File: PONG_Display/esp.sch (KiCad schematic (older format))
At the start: 13 parts, among them J8 ESP_Conn, J9 ESP_Prog_Conn, SW2 SW_Push, SW3 SW_Push_SPDT, SW4 SW_Push_SPDT

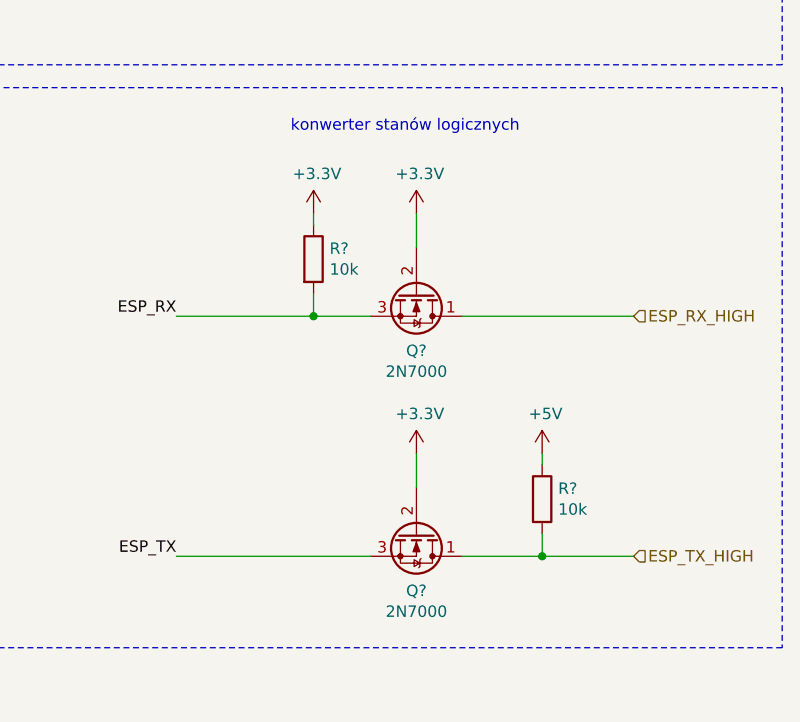
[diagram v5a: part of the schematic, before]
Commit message: dodalem rezystory i wywalilem ze zlacza zasilanie tasmy
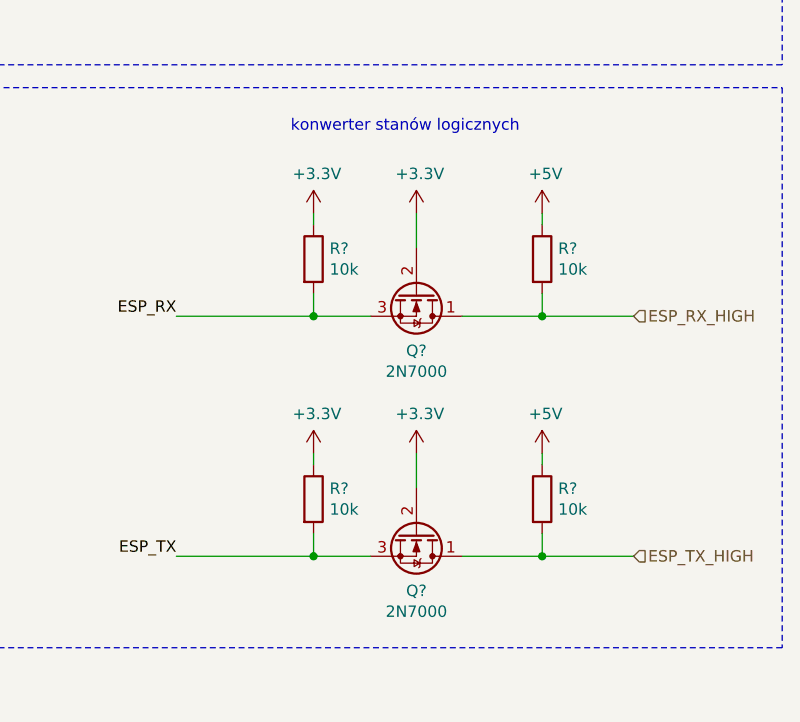
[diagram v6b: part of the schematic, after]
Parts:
- added R? (x2): 10k, Resistor_SMD:R_1206_3216Metric_Pad1.42x1.75mm_HandSolder, symbol Device:R
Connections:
- net +3V3: now also R?.1
- net +5V: now also R?.1
- net ESP_RX_HIGH: now also R?.2
- net ESP_TX: now also R?.2
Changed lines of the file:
@@
 Text Label 4350 3150 2    50   ~ 0
 ESP_RX
+$Comp
+L power:+3.3V #PWR?
+U 1 1 5E9DD25C
+P 4700 5250
+F 0 "#PWR?" H 4700 5100 50  0001 C CNN
+F 1 "+3.3V" H 4715 5423 50  0000 C CNN
+F 2 "" H 4700 5250 50  0001 C CNN
+F 3 "" H 4700 5250 50  0001 C CNN
+	1    4700 5250
+	1    0    0    -1
+$EndComp
+Wire Wire Line
+	4550 5250 4700 5250
+Wire Wire Line
+	4700 5250 4800 5250
+Connection ~ 4700 5250
 Text HLabel 10050 5050 2    50   Input ~ 0
 ESP_RX_HIGH
@@
 Text Label 8050 6100 2    50   ~ 0
 ESP_TX
+$Comp
+L power:+3.3V #PWR?
+U 1 1 5E9E0D36
+P 9100 4600
+F 0 "#PWR?" H 9100 4450 50  0001 C CNN
+F 1 "+3.3V" H 9115 4773 50  0000 C CNN
+F 2 "" H 9100 4600 50  0001 C CNN
+F 3 "" H 9100 4600 50  0001 C CNN
+	1    9100 4600
+	1    0    0    -1
+$EndComp
+$Comp
+L power:+3.3V #PWR?
+U 1 1 5E9E0F18
+P 9100 5650
+F 0 "#PWR?" H 9100 5500 50  0001 C CNN
+F 1 "+3.3V" H 9115 5823 50  0000 C CNN
+F 2 "" H 9100 5650 50  0001 C CNN
+F 3 "" H 9100 5650 50  0001 C CNN
+	1    9100 5650
+	1    0    0    -1
+$EndComp
+Wire Wire Line
+	9100 4600 9100 4750
+Wire Wire Line
+	9100 5650 9100 5800
 $Comp
 L Device:Q_NMOS_DGS Q?
@@
 	0    1    1    0
 $EndComp
+Text Notes 8550 4250 0    50   ~ 0
+konwerter stanów logicznych\n
+Connection ~ 8650 5050
+Wire Wire Line
+	8650 5050 8900 5050
 Wire Wire Line
 	8050 5050 8650 5050
-Wire Wire Line
-	9300 6100 9650 6100
+$Comp
+L Device:R R?
+U 1 1 5E9D56BD
+P 8650 4800
+F 0 "R?" H 8720 4846 50  0000 L CNN
+F 1 "10k" H 8720 4755 50  0000 L CNN
+F 2 "Resistor_SMD:R_1206_3216Metric_Pad1.42x1.75mm_HandSolder" V 8580 4800 50  0001 C CNN
+F 3 "~" H 8650 4800 50  0001 C CNN
+	1    8650 4800
+	1    0    0    -1
+$EndComp
+Wire Wire Line
+	8650 4600 8650 4650
+Wire Wire Line
+	8650 4950 8650 5050
 $Comp
 L power:+3.3V #PWR?
@@
 $EndComp
 Wire Wire Line
-	8650 4950 8650 5050
-Connection ~ 8650 5050
-Wire Wire Line
-	8650 5050 8900 5050
-Wire Wire Line
-	8650 4600 8650 4650
-$Comp
-L Device:R R?
-U 1 1 5E9D56BD
-P 8650 4800
-F 0 "R?" H 8720 4846 50  0000 L CNN
-F 1 "10k" H 8720 4755 50  0000 L CNN
-F 2 "Resistor_SMD:R_1206_3216Metric_Pad1.42x1.75mm_HandSolder" V 8580 4800 50  0001 C CNN
-F 3 "~" H 8650 4800 50  0001 C CNN
-	1    8650 4800
-	1    0    0    -1
-$EndComp
+	9300 6100 9650 6100
+Wire Wire Line
+	9650 6100 10050 6100
+Connection ~ 9650 6100
 $Comp
 L power:+5V #PWR?
@@
 Wire Wire Line
 	9650 6000 9650 6100
-Connection ~ 9650 6100
-Wire Wire Line
-	9650 6100 10050 6100
-Wire Wire Line
-	4550 5250 4700 5250
-$Comp
-L power:+3.3V #PWR?
-U 1 1 5E9DD25C
-P 4700 5250
-F 0 "#PWR?" H 4700 5100 50  0001 C CNN
-F 1 "+3.3V" H 4715 5423 50  0000 C CNN
-F 2 "" H 4700 5250 50  0001 C CNN
-F 3 "" H 4700 5250 50  0001 C CNN
-	1    4700 5250
-	1    0    0    -1
-$EndComp
-Connection ~ 4700 5250
-Wire Wire Line
-	4700 5250 4800 5250
-$Comp
-L power:+3.3V #PWR?
-U 1 1 5E9E0D36
-P 9100 4600
-F 0 "#PWR?" H 9100 4450 50  0001 C CNN
-F 1 "+3.3V" H 9115 4773 50  0000 C CNN
-F 2 "" H 9100 4600 50  0001 C CNN
-F 3 "" H 9100 4600 50  0001 C CNN
-	1    9100 4600
-	1    0    0    -1
-$EndComp
-$Comp
-L power:+3.3V #PWR?
-U 1 1 5E9E0F18
-P 9100 5650
-F 0 "#PWR?" H 9100 5500 50  0001 C CNN
-F 1 "+3.3V" H 9115 5823 50  0000 C CNN
-F 2 "" H 9100 5650 50  0001 C CNN
-F 3 "" H 9100 5650 50  0001 C CNN
-	1    9100 5650
-	1    0    0    -1
-$EndComp
-Wire Wire Line
-	9100 4600 9100 4750
-Wire Wire Line
-	9100 5650 9100 5800
-Text Notes 8550 4250 0    50   ~ 0
-konwerter stanów logicznych\n
+Wire Wire Line
+	8650 5650 8650 5700
+$Comp
+L power:+3.3V #PWR?
+U 1 1 5E9D533A
+P 8650 5650
+F 0 "#PWR?" H 8650 5500 50  0001 C CNN
+F 1 "+3.3V" H 8665 5823 50  0000 C CNN
+F 2 "" H 8650 5650 50  0001 C CNN
+F 3 "" H 8650 5650 50  0001 C CNN
+	1    8650 5650
+	1    0    0    -1
+$EndComp
+Wire Wire Line
+	8650 6100 8900 6100
+Wire Wire Line
+	8050 6100 8650 6100
+Connection ~ 8650 6100
+Wire Wire Line
+	8650 6000 8650 6100
+$Comp
+L Device:R R?
+U 1 1 5E9D5B4F
+P 8650 5850
+F 0 "R?" H 8720 5896 50  0000 L CNN
+F 1 "10k" H 8720 5805 50  0000 L CNN
+F 2 "Resistor_SMD:R_1206_3216Metric_Pad1.42x1.75mm_HandSolder" V 8580 5850 50  0001 C CNN
+F 3 "~" H 8650 5850 50  0001 C CNN
+	1    8650 5850
+	1    0    0    -1
+$EndComp
+Wire Wire Line
+	9650 5050 10050 5050
+Wire Wire Line
+	9300 5050 9650 5050
+Connection ~ 9650 5050
+Wire Wire Line
+	9650 4950 9650 5050
+$Comp
+L power:+5V #PWR?
+U 1 1 5E9D8E3B
+P 9650 4600
+F 0 "#PWR?" H 9650 4450 50  0001 C CNN
+F 1 "+5V" H 9665 4773 50  0000 C CNN
+F 2 "" H 9650 4600 50  0001 C CNN
+F 3 "" H 9650 4600 50  0001 C CNN
+	1    9650 4600
+	1    0    0    -1
+$EndComp
+Wire Wire Line
+	9650 4600 9650 4650
+$Comp
+L Device:R R?
+U 1 1 5E9D99AA
+P 9650 4800
+F 0 "R?" H 9720 4846 50  0000 L CNN
+F 1 "10k" H 9720 4755 50  0000 L CNN
+F 2 "Resistor_SMD:R_1206_3216Metric_Pad1.42x1.75mm_HandSolder" V 9580 4800 50  0001 C CNN
+F 3 "~" H 9650 4800 50  0001 C CNN
+	1    9650 4800
+	1    0    0    -1
+$EndComp
 Wire Notes Line
 	7000 4050 10700 4050
@@
 Wire Notes Line
 	7000 6500 7000 4050
-Wire Wire Line
-	9300 5050 10050 5050
-Wire Wire Line
-	8050 6100 8900 6100
 $EndSCHEMATC

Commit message: layout v1
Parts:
- removed Q? (x2): 2N7000, symbol Device:Q_NMOS_DGS
- added Q1, Q2: BSS138, Package_TO_SOT_SMD:SOT-23, symbol Transistor_FET:BSS138
- C22: footprint Capacitor_SMD:C_1206_3216Metric_Pad1.42x1.75mm_HandSolder -> Capacitor_SMD:C_0603_1608Metric_Pad1.05x0.95mm_HandSolder
- gave numbers to parts that had none: 4
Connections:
- net +3V3: now also Q1.1 (G), Q2.1 (G)
- net ESP_RX: now also Q1.2 (S)
- net ESP_RX_HIGH: now also Q1.3 (D)
- net ESP_TX: now also Q2.2 (S)
- net ESP_TX_HIGH: now also Q2.3 (D)
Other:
- note added: "Przycisk resetu układu ESP"
- moved on the sheet: C22, D4, R8, R9, SW2
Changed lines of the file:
@@
 EESchema Schematic File Version 4
-LIBS:PONG_Display-cache
 EELAYER 30 0
 EELAYER END
@@
 L power:GND #PWR065
 U 1 1 5E9DFF88
-P 4700 6250
-F 0 "#PWR065" H 4700 6000 50  0001 C CNN
-F 1 "GND" H 4705 6077 50  0000 C CNN
-F 2 "" H 4700 6250 50  0001 C CNN
-F 3 "" H 4700 6250 50  0001 C CNN
-	1    4700 6250
+P 3700 6200
+F 0 "#PWR065" H 3700 5950 50  0001 C CNN
+F 1 "GND" H 3705 6027 50  0000 C CNN
+F 2 "" H 3700 6200 50  0001 C CNN
+F 3 "" H 3700 6200 50  0001 C CNN
+	1    3700 6200
 	1    0    0    -1
 $EndComp
@@
 L Device:C C22
 U 1 1 5E9DFF8E
-P 4700 6000
-F 0 "C22" H 4815 6046 50  0000 L CNN
-F 1 "100n" H 4815 5955 50  0000 L CNN
-F 2 "Capacitor_SMD:C_1206_3216Metric_Pad1.42x1.75mm_HandSolder" H 4738 5850 50  0001 C CNN
-F 3 "~" H 4700 6000 50  0001 C CNN
-	1    4700 6000
+P 3700 5950
+F 0 "C22" H 3815 5996 50  0000 L CNN
+F 1 "100n" H 3815 5905 50  0000 L CNN
+F 2 "Capacitor_SMD:C_0603_1608Metric_Pad1.05x0.95mm_HandSolder" H 3738 5800 50  0001 C CNN
+F 3 "~" H 3700 5950 50  0001 C CNN
+	1    3700 5950
 	1    0    0    -1
 $EndComp
@@
 L Device:R R8
 U 1 1 5E9DFF94
-P 4550 5500
-F 0 "R8" H 4620 5546 50  0000 L CNN
-F 1 "10k" H 4620 5455 50  0000 L CNN
-F 2 "Resistor_SMD:R_1206_3216Metric_Pad1.42x1.75mm_HandSolder" V 4480 5500 50  0001 C CNN
-F 3 "~" H 4550 5500 50  0001 C CNN
-	1    4550 5500
+P 3550 5450
+F 0 "R8" H 3620 5496 50  0000 L CNN
+F 1 "10k" H 3620 5405 50  0000 L CNN
+F 2 "Resistor_SMD:R_1206_3216Metric_Pad1.42x1.75mm_HandSolder" V 3480 5450 50  0001 C CNN
+F 3 "~" H 3550 5450 50  0001 C CNN
+	1    3550 5450
 	1    0    0    -1
 $EndComp
@@
 L Device:D_Zener D4
 U 1 1 5E9DFF9A
-P 4800 5500
-F 0 "D4" V 4754 5579 50  0000 L CNN
-F 1 "D_Zener" V 4845 5579 50  0000 L CNN
-F 2 "Diode_THT:D_DO-34_SOD68_P7.62mm_Horizontal" H 4800 5500 50  0001 C CNN
-F 3 "~" H 4800 5500 50  0001 C CNN
-	1    4800 5500
+P 3800 5450
+F 0 "D4" V 3754 5529 50  0000 L CNN
+F 1 "D_Zener" V 3845 5529 50  0000 L CNN
+F 2 "Diode_THT:D_DO-34_SOD68_P7.62mm_Horizontal" H 3800 5450 50  0001 C CNN
+F 3 "~" H 3800 5450 50  0001 C CNN
+	1    3800 5450
 	0    1    1    0
 $EndComp
 Wire Wire Line
-	4800 5250 4800 5350
-Wire Wire Line
-	4550 5250 4550 5350
-Wire Wire Line
-	4550 5650 4550 5750
-Wire Wire Line
-	4800 5750 4800 5650
-Wire Wire Line
-	4700 6250 4700 6150
-Wire Wire Line
-	4550 5750 4050 5750
-Connection ~ 4550 5750
+	3800 5200 3800 5300
+Wire Wire Line
+	3550 5200 3550 5300
+Wire Wire Line
+	3550 5600 3550 5700
+Wire Wire Line
+	3800 5700 3800 5600
+Wire Wire Line
+	3700 6200 3700 6100
+Wire Wire Line
+	3550 5700 3050 5700
+Connection ~ 3550 5700
 $Comp
 L Device:R R9
 U 1 1 5E9DFFAA
-P 5850 6100
-F 0 "R9" H 5920 6146 50  0000 L CNN
-F 1 "330R" H 5920 6055 50  0000 L CNN
-F 2 "Resistor_SMD:R_1206_3216Metric_Pad1.42x1.75mm_HandSolder" V 5780 6100 50  0001 C CNN
-F 3 "~" H 5850 6100 50  0001 C CNN
-	1    5850 6100
+P 4850 6050
+F 0 "R9" H 4920 6096 50  0000 L CNN
+F 1 "330R" H 4920 6005 50  0000 L CNN
+F 2 "Resistor_SMD:R_1206_3216Metric_Pad1.42x1.75mm_HandSolder" V 4780 6050 50  0001 C CNN
+F 3 "~" H 4850 6050 50  0001 C CNN
+	1    4850 6050
 	1    0    0    -1
 $EndComp
@@
 L power:GND #PWR067
 U 1 1 5E9DFFB0
-P 5850 6500
-F 0 "#PWR067" H 5850 6250 50  0001 C CNN
-F 1 "GND" H 5855 6327 50  0000 C CNN
-F 2 "" H 5850 6500 50  0001 C CNN
-F 3 "" H 5850 6500 50  0001 C CNN
-	1    5850 6500
-	1    0    0    -1
-$EndComp
-Wire Wire Line
-	5850 6250 5850 6500
-Wire Wire Line
-	4550 5750 4700 5750
-Wire Wire Line
-	4700 5750 4700 5850
-Connection ~ 4700 5750
-Wire Wire Line
-	4700 5750 4800 5750
+P 4850 6450
+F 0 "#PWR067" H 4850 6200 50  0001 C CNN
+F 1 "GND" H 4855 6277 50  0000 C CNN
+F 2 "" H 4850 6450 50  0001 C CNN
+F 3 "" H 4850 6450 50  0001 C CNN
+	1    4850 6450
+	1    0    0    -1
+$EndComp
+Wire Wire Line
+	4850 6200 4850 6450
+Wire Wire Line
+	3550 5700 3700 5700
+Wire Wire Line
+	3700 5700 3700 5800
+Connection ~ 3700 5700
+Wire Wire Line
+	3700 5700 3800 5700
 $Comp
 L Switch:SW_Push SW2
 U 1 1 5E9DFFBB
-P 5400 5750
-F 0 "SW2" H 5400 6035 50  0000 C CNN
-F 1 "SW_Push" H 5400 5944 50  0000 C CNN
-F 2 "Button_Switch_THT:SW_PUSH_6mm" H 5400 5950 50  0001 C CNN
-F 3 "~" H 5400 5950 50  0001 C CNN
-	1    5400 5750
-	1    0    0    -1
-$EndComp
-Wire Wire Line
-	4800 5750 5200 5750
-Connection ~ 4800 5750
-Wire Wire Line
-	5850 5750 5850 5950
-Wire Wire Line
-	5600 5750 5850 5750
-Text HLabel 4050 5750 0    50   Input ~ 0
+P 4400 5700
+F 0 "SW2" H 4400 5985 50  0000 C CNN
+F 1 "SW_Push" H 4400 5894 50  0000 C CNN
+F 2 "Button_Switch_THT:SW_PUSH_6mm" H 4400 5900 50  0001 C CNN
+F 3 "~" H 4400 5900 50  0001 C CNN
+	1    4400 5700
+	1    0    0    -1
+$EndComp
+Wire Wire Line
+	3800 5700 4200 5700
+Connection ~ 3800 5700
+Wire Wire Line
+	4850 5700 4850 5900
+Wire Wire Line
+	4600 5700 4850 5700
+Text HLabel 3050 5700 0    50   Input ~ 0
 ESP_RST
 Wire Wire Line
@@
 ESP_RX
 $Comp
-L power:+3.3V #PWR?
+L power:+3.3V #PWR0101
 U 1 1 5E9DD25C
-P 4700 5250
-F 0 "#PWR?" H 4700 5100 50  0001 C CNN
-F 1 "+3.3V" H 4715 5423 50  0000 C CNN
-F 2 "" H 4700 5250 50  0001 C CNN
-F 3 "" H 4700 5250 50  0001 C CNN
-	1    4700 5250
-	1    0    0    -1
-$EndComp
-Wire Wire Line
-	4550 5250 4700 5250
-Wire Wire Line
-	4700 5250 4800 5250
-Connection ~ 4700 5250
+P 3700 5200
+F 0 "#PWR0101" H 3700 5050 50  0001 C CNN
+F 1 "+3.3V" H 3715 5373 50  0000 C CNN
+F 2 "" H 3700 5200 50  0001 C CNN
+F 3 "" H 3700 5200 50  0001 C CNN
+	1    3700 5200
+	1    0    0    -1
+$EndComp
+Wire Wire Line
+	3550 5200 3700 5200
+Wire Wire Line
+	3700 5200 3800 5200
+Connection ~ 3700 5200
 Text HLabel 10050 5050 2    50   Input ~ 0
 ESP_RX_HIGH
@@
 ESP_TX
 $Comp
-L power:+3.3V #PWR?
+L power:+3.3V #PWR0102
 U 1 1 5E9E0D36
 P 9100 4600
-F 0 "#PWR?" H 9100 4450 50  0001 C CNN
+F 0 "#PWR0102" H 9100 4450 50  0001 C CNN
 F 1 "+3.3V" H 9115 4773 50  0000 C CNN
 F 2 "" H 9100 4600 50  0001 C CNN
@@
 $EndComp
 $Comp
-L power:+3.3V #PWR?
+L power:+3.3V #PWR0103
 U 1 1 5E9E0F18
 P 9100 5650
-F 0 "#PWR?" H 9100 5500 50  0001 C CNN
+F 0 "#PWR0103" H 9100 5500 50  0001 C CNN
 F 1 "+3.3V" H 9115 5823 50  0000 C CNN
 F 2 "" H 9100 5650 50  0001 C CNN
@@
 Wire Wire Line
 	9100 5650 9100 5800
-$Comp
-L Device:Q_NMOS_DGS Q?
-U 1 1 5E9CF246
-P 9100 4950
-F 0 "Q?" V 9351 4950 50  0000 C CNN
-F 1 "2N7000" V 9442 4950 50  0000 C CNN
-F 2 "" H 9300 5050 50  0001 C CNN
-F 3 "~" H 9100 4950 50  0001 C CNN
-	1    9100 4950
-	0    1    1    0
-$EndComp
-$Comp
-L Device:Q_NMOS_DGS Q?
-U 1 1 5E9D0B65
-P 9100 6000
-F 0 "Q?" V 9351 6000 50  0000 C CNN
-F 1 "2N7000" V 9442 6000 50  0000 C CNN
-F 2 "" H 9300 6100 50  0001 C CNN
-F 3 "~" H 9100 6000 50  0001 C CNN
-	1    9100 6000
-	0    1    1    0
-$EndComp
 Text Notes 8550 4250 0    50   ~ 0
 konwerter stanów logicznych\n
@@
 	8050 5050 8650 5050
 $Comp
-L Device:R R?
+L Device:R R10
 U 1 1 5E9D56BD
 P 8650 4800
-F 0 "R?" H 8720 4846 50  0000 L CNN
+F 0 "R10" H 8720 4846 50  0000 L CNN
 F 1 "10k" H 8720 4755 50  0000 L CNN
 F 2 "Resistor_SMD:R_1206_3216Metric_Pad1.42x1.75mm_HandSolder" V 8580 4800 50  0001 C CNN
@@
 	8650 4950 8650 5050
 $Comp
-L power:+3.3V #PWR?
+L power:+3.3V #PWR0104
 U 1 1 5E9D4B92
 P 8650 4600
-F 0 "#PWR?" H 8650 4450 50  0001 C CNN
+F 0 "#PWR0104" H 8650 4450 50  0001 C CNN
 F 1 "+3.3V" H 8665 4773 50  0000 C CNN
 F 2 "" H 8650 4600 50  0001 C CNN
@@
 Connection ~ 9650 6100
 $Comp
-L power:+5V #PWR?
+L power:+5V #PWR0105
 U 1 1 5E9D96BA
 P 9650 5650
-F 0 "#PWR?" H 9650 5500 50  0001 C CNN
+F 0 "#PWR0105" H 9650 5500 50  0001 C CNN
 F 1 "+5V" H 9665 5823 50  0000 C CNN
 F 2 "" H 9650 5650 50  0001 C CNN
@@
 $EndComp
 $Comp
-L Device:R R?
+L Device:R R13
 U 1 1 5E9D9C8C
 P 9650 5850
-F 0 "R?" H 9720 5896 50  0000 L CNN
+F 0 "R13" H 9720 5896 50  0000 L CNN
 F 1 "10k" H 9720 5805 50  0000 L CNN
 F 2 "Resistor_SMD:R_1206_3216Metric_Pad1.42x1.75mm_HandSolder" V 9580 5850 50  0001 C CNN
@@
 	8650 5650 8650 5700
 $Comp
-L power:+3.3V #PWR?
+L power:+3.3V #PWR0106
 U 1 1 5E9D533A
 P 8650 5650
-F 0 "#PWR?" H 8650 5500 50  0001 C CNN
+F 0 "#PWR0106" H 8650 5500 50  0001 C CNN
 F 1 "+3.3V" H 8665 5823 50  0000 C CNN
 F 2 "" H 8650 5650 50  0001 C CNN
@@
 	8650 6000 8650 6100
 $Comp
-L Device:R R?
+L Device:R R11
 U 1 1 5E9D5B4F
 P 8650 5850
-F 0 "R?" H 8720 5896 50  0000 L CNN
+F 0 "R11" H 8720 5896 50  0000 L CNN
 F 1 "10k" H 8720 5805 50  0000 L CNN
 F 2 "Resistor_SMD:R_1206_3216Metric_Pad1.42x1.75mm_HandSolder" V 8580 5850 50  0001 C CNN
@@
 	9650 4950 9650 5050
 $Comp
-L power:+5V #PWR?
+L power:+5V #PWR0107
 U 1 1 5E9D8E3B
 P 9650 4600
-F 0 "#PWR?" H 9650 4450 50  0001 C CNN
+F 0 "#PWR0107" H 9650 4450 50  0001 C CNN
 F 1 "+5V" H 9665 4773 50  0000 C CNN
 F 2 "" H 9650 4600 50  0001 C CNN
@@
 	9650 4600 9650 4650
 $Comp
-L Device:R R?
+L Device:R R12
 U 1 1 5E9D99AA
 P 9650 4800
-F 0 "R?" H 9720 4846 50  0000 L CNN
+F 0 "R12" H 9720 4846 50  0000 L CNN
 F 1 "10k" H 9720 4755 50  0000 L CNN
 F 2 "Resistor_SMD:R_1206_3216Metric_Pad1.42x1.75mm_HandSolder" V 9580 4800 50  0001 C CNN
@@
 Wire Notes Line
 	7000 6500 7000 4050
+$Comp
+L Transistor_FET:BSS138 Q1
+U 1 1 5EA53259
+P 9100 4950
+F 0 "Q1" V 9349 4950 50  0000 C CNN
+F 1 "BSS138" V 9440 4950 50  0000 C CNN
+F 2 "Package_TO_SOT_SMD:SOT-23" H 9300 4875 50  0001 L CIN
+F 3 "https://www.fairchildsemi.com/datasheets/BS/BSS138.pdf" H 9100 4950 50  0001 L CNN
+	1    9100 4950
+	0    1    1    0
+$EndComp
+$Comp
+L Transistor_FET:BSS138 Q2
+U 1 1 5EA59994
+P 9100 6000
+F 0 "Q2" V 9349 6000 50  0000 C CNN
+F 1 "BSS138" V 9440 6000 50  0000 C CNN
+F 2 "Package_TO_SOT_SMD:SOT-23" H 9300 5925 50  0001 L CIN
+F 3 "https://www.fairchildsemi.com/datasheets/BS/BSS138.pdf" H 9100 6000 50  0001 L CNN
+	1    9100 6000
+	0    1    1    0
+$EndComp
+Wire Notes Line
+	2150 4450 6000 4450
+Wire Notes Line
+	6000 4450 6000 7250
+Wire Notes Line
+	6000 7250 2150 7250
+Wire Notes Line
+	2150 7250 2150 4450
+Text Notes 3500 4650 0    50   ~ 0
+Przycisk resetu układu ESP
 $EndSCHEMATC

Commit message: l
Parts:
- R10, R11, R12, R13, R8, R9: footprint Resistor_SMD:R_1206_3216Metric_Pad1.42x1.75mm_HandSolder -> Resistor_SMD:R_0603_1608Metric_Pad1.05x0.95mm_HandSolder
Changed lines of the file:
@@
 F 0 "R8" H 3620 5496 50  0000 L CNN
 F 1 "10k" H 3620 5405 50  0000 L CNN
-F 2 "Resistor_SMD:R_1206_3216Metric_Pad1.42x1.75mm_HandSolder" V 3480 5450 50  0001 C CNN
+F 2 "Resistor_SMD:R_0603_1608Metric_Pad1.05x0.95mm_HandSolder" V 3480 5450 50  0001 C CNN
 F 3 "~" H 3550 5450 50  0001 C CNN
 	1    3550 5450
@@
 F 0 "R9" H 4920 6096 50  0000 L CNN
 F 1 "330R" H 4920 6005 50  0000 L CNN
-F 2 "Resistor_SMD:R_1206_3216Metric_Pad1.42x1.75mm_HandSolder" V 4780 6050 50  0001 C CNN
+F 2 "Resistor_SMD:R_0603_1608Metric_Pad1.05x0.95mm_HandSolder" V 4780 6050 50  0001 C CNN
 F 3 "~" H 4850 6050 50  0001 C CNN
 	1    4850 6050
@@
 F 0 "R10" H 8720 4846 50  0000 L CNN
 F 1 "10k" H 8720 4755 50  0000 L CNN
-F 2 "Resistor_SMD:R_1206_3216Metric_Pad1.42x1.75mm_HandSolder" V 8580 4800 50  0001 C CNN
+F 2 "Resistor_SMD:R_0603_1608Metric_Pad1.05x0.95mm_HandSolder" V 8580 4800 50  0001 C CNN
 F 3 "~" H 8650 4800 50  0001 C CNN
 	1    8650 4800
@@
 F 0 "R13" H 9720 5896 50  0000 L CNN
 F 1 "10k" H 9720 5805 50  0000 L CNN
-F 2 "Resistor_SMD:R_1206_3216Metric_Pad1.42x1.75mm_HandSolder" V 9580 5850 50  0001 C CNN
+F 2 "Resistor_SMD:R_0603_1608Metric_Pad1.05x0.95mm_HandSolder" V 9580 5850 50  0001 C CNN
 F 3 "~" H 9650 5850 50  0001 C CNN
 	1    9650 5850
@@
 F 0 "R11" H 8720 5896 50  0000 L CNN
 F 1 "10k" H 8720 5805 50  0000 L CNN
-F 2 "Resistor_SMD:R_1206_3216Metric_Pad1.42x1.75mm_HandSolder" V 8580 5850 50  0001 C CNN
+F 2 "Resistor_SMD:R_0603_1608Metric_Pad1.05x0.95mm_HandSolder" V 8580 5850 50  0001 C CNN
 F 3 "~" H 8650 5850 50  0001 C CNN
 	1    8650 5850
@@
 F 0 "R12" H 9720 4846 50  0000 L CNN
 F 1 "10k" H 9720 4755 50  0000 L CNN
-F 2 "Resistor_SMD:R_1206_3216Metric_Pad1.42x1.75mm_HandSolder" V 9580 4800 50  0001 C CNN
+F 2 "Resistor_SMD:R_0603_1608Metric_Pad1.05x0.95mm_HandSolder" V 9580 4800 50  0001 C CNN
 F 3 "~" H 9650 4800 50  0001 C CNN
 	1    9650 4800
